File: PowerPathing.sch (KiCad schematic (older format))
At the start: 23 parts, among them IC1 LTC4372IMS8#TRPBF, IC2 L4940D2T12-TR, IC3 MAX738ACWE+, Q1 BSC026NE2LS5ATMA1

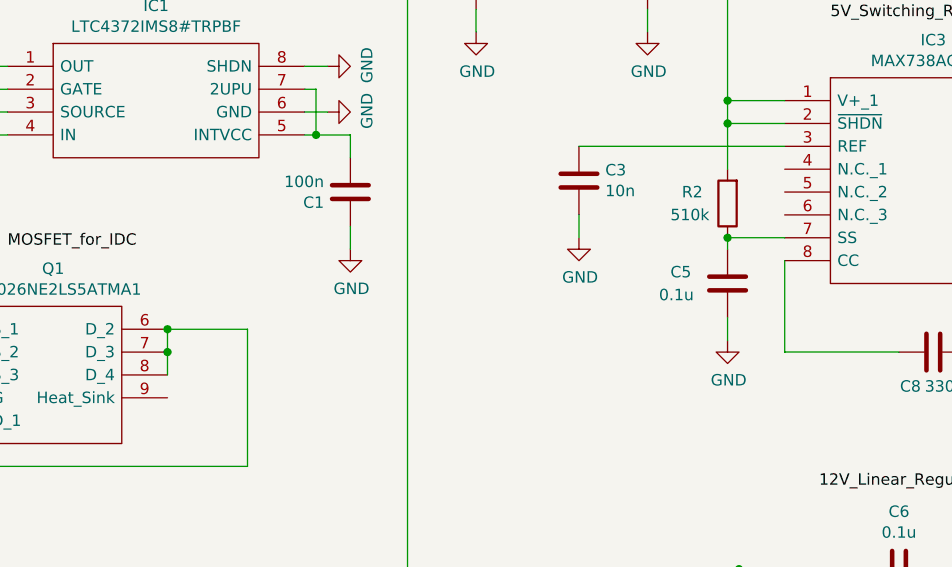
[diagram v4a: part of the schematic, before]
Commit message: added connector to schematic
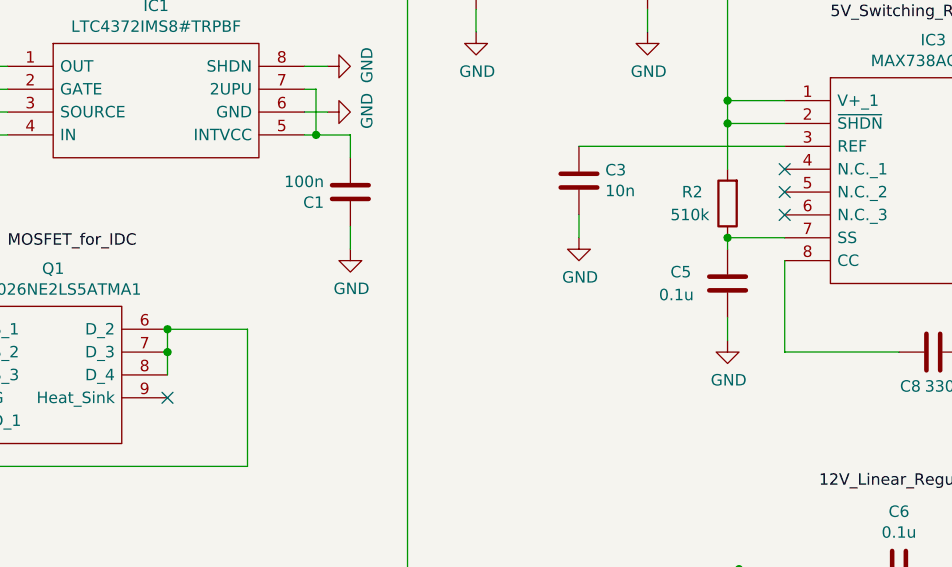
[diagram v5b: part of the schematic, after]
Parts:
- C1, C3, C5, C6, C8: footprint (none) -> Capacitor_SMD:C_0805_2012Metric_Pad1.18x1.45mm_HandSolder
- D1: footprint (none) -> Diode_SMD:D_0805_2012Metric_Pad1.15x1.40mm_HandSolder
- R1, R2: footprint (none) -> Resistor_SMD:R_0805_2012Metric_Pad1.20x1.40mm_HandSolder
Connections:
- no-connect marks 0 -> 4
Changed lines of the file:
@@
 F 0 "C3" H 4865 2846 50  0000 L CNN
 F 1 "10n" H 4865 2755 50  0000 L CNN
-F 2 "" H 4788 2650 50  0001 C CNN
+F 2 "Capacitor_SMD:C_0805_2012Metric_Pad1.18x1.45mm_HandSolder" H 4788 2650 50  0001 C CNN
 F 3 "~" H 4750 2800 50  0001 C CNN
 	1    4750 2800
@@
 F 0 "R2" H 5600 2850 50  0000 R CNN
 F 1 "510k" H 5650 2950 50  0000 R CNN
-F 2 "" V 5330 2900 50  0001 C CNN
+F 2 "Resistor_SMD:R_0805_2012Metric_Pad1.20x1.40mm_HandSolder" V 5330 2900 50  0001 C CNN
 F 3 "~" H 5400 2900 50  0001 C CNN
 	1    5400 2900
@@
 F 0 "C5" H 5150 3300 50  0000 L CNN
 F 1 "0.1u" H 5100 3200 50  0000 L CNN
-F 2 "" H 5438 3100 50  0001 C CNN
+F 2 "Capacitor_SMD:C_0805_2012Metric_Pad1.18x1.45mm_HandSolder" H 5438 3100 50  0001 C CNN
 F 3 "~" H 5400 3250 50  0001 C CNN
 	1    5400 3250
@@
 F 0 "C8" V 6450 3450 50  0000 C CNN
 F 1 "330p" V 6450 3600 50  0000 C CNN
-F 2 "" H 6338 3400 50  0001 C CNN
+F 2 "Capacitor_SMD:C_0805_2012Metric_Pad1.18x1.45mm_HandSolder" H 6338 3400 50  0001 C CNN
 F 3 "~" H 6300 3550 50  0001 C CNN
 	1    6300 3550
@@
 F 0 "C6" V 5898 4500 50  0000 C CNN
 F 1 "0.1u" V 5989 4500 50  0000 C CNN
-F 2 "" H 6188 4350 50  0001 C CNN
+F 2 "Capacitor_SMD:C_0805_2012Metric_Pad1.18x1.45mm_HandSolder" H 6188 4350 50  0001 C CNN
 F 3 "~" H 6150 4500 50  0001 C CNN
 	1    6150 4500
@@
 F 0 "C1" H 3865 2896 50  0000 L CNN
 F 1 "100n" H 3865 2805 50  0000 L CNN
-F 2 "" H 3788 2700 50  0001 C CNN
+F 2 "Capacitor_SMD:C_0805_2012Metric_Pad1.18x1.45mm_HandSolder" H 3788 2700 50  0001 C CNN
 F 3 "~" H 3750 2850 50  0001 C CNN
 	1    3750 2850
@@
 F 0 "R1" H 1670 2096 50  0000 L CNN
 F 1 "111 ohms" H 1670 2005 50  0000 L CNN
-F 2 "" V 1530 2050 50  0001 C CNN
+F 2 "Resistor_SMD:R_0805_2012Metric_Pad1.20x1.40mm_HandSolder" V 1530 2050 50  0001 C CNN
 F 3 "~" H 1600 2050 50  0001 C CNN
 	1    1600 2050
@@
 F 0 "D1" H 1300 1533 50  0000 C CNN
 F 1 "1N4001G" H 1300 1624 50  0000 C CNN
-F 2 "" H 1300 1750 50  0001 C CNN
+F 2 "Diode_SMD:D_0805_2012Metric_Pad1.15x1.40mm_HandSolder" H 1300 1750 50  0001 C CNN
 F 3 "~" H 1300 1750 50  0001 C CNN
 	1    1300 1750
@@
 Text Label 2250 3100 0    50   ~ 0
 MOSFET_for_IDC
+NoConn ~ 2950 3750
+NoConn ~ 5650 2950
+NoConn ~ 5650 2850
+NoConn ~ 5650 2750
 $EndSCHEMATC

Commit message: Started schematic development
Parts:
- removed C4: 1u, symbol Device:CP
- added C4: 860020672005, CAPPRD200W52D500H1250, symbol Capstone:860020672005
- C1, C3, C5, C6, C8: footprint Capacitor_SMD:C_0805_2012Metric_Pad1.18x1.45mm_HandSolder -> Capacitor_THT:C_Rect_L7.0mm_W2.5mm_P5.00mm
- C2: footprint (none) -> CAPPRD200W52D500H1250
- C7, C9: footprint (none) -> Capstone:CAPPRD200W52D500H1250
- R1: value 111 ohms -> 111; footprint Resistor_SMD:R_0805_2012Metric_Pad1.20x1.40mm_HandSolder -> Resistor_THT:R_Axial_DIN0204_L3.6mm_D1.6mm_P7.62mm_Horizontal
- R2: footprint Resistor_SMD:R_0805_2012Metric_Pad1.20x1.40mm_HandSolder -> Resistor_THT:R_Axial_DIN0204_L3.6mm_D1.6mm_P7.62mm_Horizontal
- TP1, TP2, TP3, TP4, TP5: footprint (none) -> TestPoint:TestPoint_Loop_D2.60mm_Drill1.6mm_Beaded
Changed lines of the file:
@@
 F 0 "C9" H 9518 2946 50  0000 L CNN
 F 1 "100u" H 9518 2855 50  0000 L CNN
-F 2 "" H 9438 2750 50  0001 C CNN
+F 2 "Capstone:CAPPRD200W52D500H1250" H 9438 2750 50  0001 C CNN
 F 3 "~" H 9400 2900 50  0001 C CNN
 	1    9400 2900
 	1    0    0    -1
 $EndComp
-$Comp
-L Device:CP C4
-U 1 1 61549C3D
-P 5050 1900
-F 0 "C4" H 5168 1946 50  0000 L CNN
-F 1 "1u" H 5168 1855 50  0000 L CNN
-F 2 "" H 5088 1750 50  0001 C CNN
-F 3 "~" H 5050 1900 50  0001 C CNN
-	1    5050 1900
-	1    0    0    -1
-$EndComp
-Wire Wire Line
-	5050 1750 5400 1750
 Wire Wire Line
 	5400 1750 5400 2450
 Wire Wire Line
 	5400 2450 5650 2450
-Connection ~ 5050 1750
 Wire Wire Line
 	5650 2550 5400 2550
@@
 F 0 "C3" H 4865 2846 50  0000 L CNN
 F 1 "10n" H 4865 2755 50  0000 L CNN
-F 2 "Capacitor_SMD:C_0805_2012Metric_Pad1.18x1.45mm_HandSolder" H 4788 2650 50  0001 C CNN
+F 2 "Capacitor_THT:C_Rect_L7.0mm_W2.5mm_P5.00mm" H 4788 2650 50  0001 C CNN
 F 3 "~" H 4750 2800 50  0001 C CNN
 	1    4750 2800
@@
 F 0 "R2" H 5600 2850 50  0000 R CNN
 F 1 "510k" H 5650 2950 50  0000 R CNN
-F 2 "Resistor_SMD:R_0805_2012Metric_Pad1.20x1.40mm_HandSolder" V 5330 2900 50  0001 C CNN
+F 2 "Resistor_THT:R_Axial_DIN0204_L3.6mm_D1.6mm_P7.62mm_Horizontal" V 5330 2900 50  0001 C CNN
 F 3 "~" H 5400 2900 50  0001 C CNN
 	1    5400 2900
@@
 F 0 "C5" H 5150 3300 50  0000 L CNN
 F 1 "0.1u" H 5100 3200 50  0000 L CNN
-F 2 "Capacitor_SMD:C_0805_2012Metric_Pad1.18x1.45mm_HandSolder" H 5438 3100 50  0001 C CNN
+F 2 "Capacitor_THT:C_Rect_L7.0mm_W2.5mm_P5.00mm" H 5438 3100 50  0001 C CNN
 F 3 "~" H 5400 3250 50  0001 C CNN
 	1    5400 3250
@@
 F 0 "C8" V 6450 3450 50  0000 C CNN
 F 1 "330p" V 6450 3600 50  0000 C CNN
-F 2 "Capacitor_SMD:C_0805_2012Metric_Pad1.18x1.45mm_HandSolder" H 6338 3400 50  0001 C CNN
+F 2 "Capacitor_THT:C_Rect_L7.0mm_W2.5mm_P5.00mm" H 6338 3400 50  0001 C CNN
 F 3 "~" H 6300 3550 50  0001 C CNN
 	1    6300 3550
@@
 F 0 "C6" V 5898 4500 50  0000 C CNN
 F 1 "0.1u" V 5989 4500 50  0000 C CNN
-F 2 "Capacitor_SMD:C_0805_2012Metric_Pad1.18x1.45mm_HandSolder" H 6188 4350 50  0001 C CNN
+F 2 "Capacitor_THT:C_Rect_L7.0mm_W2.5mm_P5.00mm" H 6188 4350 50  0001 C CNN
 F 3 "~" H 6150 4500 50  0001 C CNN
 	1    6150 4500
@@
 F 0 "C7" V 5900 5350 50  0000 C CNN
 F 1 "22u" V 6000 5350 50  0000 C CNN
-F 2 "" H 6188 5200 50  0001 C CNN
+F 2 "Capstone:CAPPRD200W52D500H1250" H 6188 5200 50  0001 C CNN
 F 3 "~" H 6150 5350 50  0001 C CNN
 	1    6150 5350
@@
 F 0 "C2" H 4418 1946 50  0000 L CNN
 F 1 "68u" H 4418 1855 50  0000 L CNN
-F 2 "" H 4338 1750 50  0001 C CNN
+F 2 "CAPPRD200W52D500H1250" H 4338 1750 50  0001 C CNN
 F 3 "~" H 4300 1900 50  0001 C CNN
 	1    4300 1900
@@
 $EndComp
 Connection ~ 4300 1750
-Wire Wire Line
-	4300 1750 5050 1750
 $Comp
 L Capstone:LTC4372IMS8#TRPBF IC1
@@
 F 0 "C1" H 3865 2896 50  0000 L CNN
 F 1 "100n" H 3865 2805 50  0000 L CNN
-F 2 "Capacitor_SMD:C_0805_2012Metric_Pad1.18x1.45mm_HandSolder" H 3788 2700 50  0001 C CNN
+F 2 "Capacitor_THT:C_Rect_L7.0mm_W2.5mm_P5.00mm" H 3788 2700 50  0001 C CNN
 F 3 "~" H 3750 2850 50  0001 C CNN
 	1    3750 2850
@@
 P 1600 2050
 F 0 "R1" H 1670 2096 50  0000 L CNN
-F 1 "111 ohms" H 1670 2005 50  0000 L CNN
-F 2 "Resistor_SMD:R_0805_2012Metric_Pad1.20x1.40mm_HandSolder" V 1530 2050 50  0001 C CNN
+F 1 "111" H 1670 2005 50  0000 L CNN
+F 2 "Resistor_THT:R_Axial_DIN0204_L3.6mm_D1.6mm_P7.62mm_Horizontal" V 1530 2050 50  0001 C CNN
 F 3 "~" H 1600 2050 50  0001 C CNN
 	1    1600 2050
@@
 F 0 "TP2" H 4192 5276 50  0000 R CNN
 F 1 "TestPoint - 12V Reg" H 4192 5367 50  0000 R CNN
-F 2 "" H 4450 5250 50  0001 C CNN
+F 2 "TestPoint:TestPoint_Loop_D2.60mm_Drill1.6mm_Beaded" H 4450 5250 50  0001 C CNN
 F 3 "~" H 4450 5250 50  0001 C CNN
 	1    4250 5250
@@
 F 0 "TP5" H 10208 2718 50  0000 L CNN
 F 1 "TestPoint - 5V Reg" H 10208 2627 50  0000 L CNN
-F 2 "" H 10350 2600 50  0001 C CNN
+F 2 "TestPoint:TestPoint_Loop_D2.60mm_Drill1.6mm_Beaded" H 10350 2600 50  0001 C CNN
 F 3 "~" H 10350 2600 50  0001 C CNN
 	1    10150 2600
@@
 F 0 "TP1" H 3658 1668 50  0000 L CNN
 F 1 "TestPoint - Power Circuit Out" H 3658 1577 50  0000 L CNN
-F 2 "" H 3800 1550 50  0001 C CNN
+F 2 "TestPoint:TestPoint_Loop_D2.60mm_Drill1.6mm_Beaded" H 3800 1550 50  0001 C CNN
 F 3 "~" H 3800 1550 50  0001 C CNN
 	1    3600 1550
@@
 L power:GND #PWR0105
 U 1 1 616ACF0A
-P 5050 2150
-F 0 "#PWR0105" H 5050 1900 50  0001 C CNN
-F 1 "GND" H 5055 1977 50  0000 C CNN
-F 2 "" H 5050 2150 50  0001 C CNN
-F 3 "" H 5050 2150 50  0001 C CNN
-	1    5050 2150
-	1    0    0    -1
-$EndComp
-Wire Wire Line
-	5050 2150 5050 2050
+P 5050 2300
+F 0 "#PWR0105" H 5050 2050 50  0001 C CNN
+F 1 "GND" H 5055 2127 50  0000 C CNN
+F 2 "" H 5050 2300 50  0001 C CNN
+F 3 "" H 5050 2300 50  0001 C CNN
+	1    5050 2300
+	1    0    0    -1
+$EndComp
 $Comp
 L power:GND #PWR0106
@@
 F 0 "TP4" H 7000 3400 50  0000 L CNN
 F 1 "GND 5V Reg" H 6800 3500 50  0000 L CNN
-F 2 "" H 7400 3250 50  0001 C CNN
+F 2 "TestPoint:TestPoint_Loop_D2.60mm_Drill1.6mm_Beaded" H 7400 3250 50  0001 C CNN
 F 3 "~" H 7400 3250 50  0001 C CNN
 	1    7200 3250
@@
 F 0 "TP3" V 7104 5338 50  0000 L CNN
 F 1 "GND 12V Reg" V 7195 5338 50  0000 L CNN
-F 2 "" H 7350 5150 50  0001 C CNN
+F 2 "TestPoint:TestPoint_Loop_D2.60mm_Drill1.6mm_Beaded" H 7350 5150 50  0001 C CNN
 F 3 "~" H 7350 5150 50  0001 C CNN
 	1    7150 5150
@@
 NoConn ~ 5650 2850
 NoConn ~ 5650 2750
+Wire Wire Line
+	4300 1750 5050 1750
+$Comp
+L Capstone:860020672005 C4
+U 1 1 61629E3D
+P 5050 1750
+F 0 "C4" V 5250 1500 50  0000 L CNN
+F 1 "860020672005" V 5400 1100 50  0000 L CNN
+F 2 "CAPPRD200W52D500H1250" H 5400 1800 50  0001 L CNN
+F 3 "https://componentsearchengine.com/Datasheets/2/860020672005.pdf" H 5400 1700 50  0001 L CNN
+F 4 "Wurth Elektronik 1uF 50 V dc Aluminium Electrolytic Capacitor, WCAP-ATG5 Series 2000h 5 (Dia.) x 11mm" H 5400 1600 50  0001 L CNN "Description"
+F 5 "12.5" H 5400 1500 50  0001 L CNN "Height"
+F 6 "Wurth Elektronik" H 5400 1400 50  0001 L CNN "Manufacturer_Name"
+F 7 "860020672005" H 5400 1300 50  0001 L CNN "Manufacturer_Part_Number"
+F 8 "710-860020672005" H 5400 1200 50  0001 L CNN "Mouser Part Number"
+F 9 "https://www.mouser.co.uk/ProductDetail/Wurth-Elektronik/860020672005?qs=0KOYDY2FL29w5cS8aahRvQ%3D%3D" H 5400 1100 50  0001 L CNN "Mouser Price/Stock"
+F 10 "" H 5400 1000 50  0001 L CNN "Arrow Part Number"
+F 11 "" H 5400 900 50  0001 L CNN "Arrow Price/Stock"
+	1    5050 1750
+	0    1    1    0
+$EndComp
+Connection ~ 5050 1750
+Wire Wire Line
+	5050 1750 5400 1750
+Wire Wire Line
+	5050 2300 5050 2250
 $EndSCHEMATC

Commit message: initial commit for layout
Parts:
- R1, R2: footprint Resistor_THT:R_Axial_DIN0204_L3.6mm_D1.6mm_P7.62mm_Horizontal -> Capstone:RESAD1650W60L650D250
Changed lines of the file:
@@
 F 0 "R2" H 5600 2850 50  0000 R CNN
 F 1 "510k" H 5650 2950 50  0000 R CNN
-F 2 "Resistor_THT:R_Axial_DIN0204_L3.6mm_D1.6mm_P7.62mm_Horizontal" V 5330 2900 50  0001 C CNN
+F 2 "Capstone:RESAD1650W60L650D250" V 5330 2900 50  0001 C CNN
 F 3 "~" H 5400 2900 50  0001 C CNN
 	1    5400 2900
@@
 F 0 "R1" H 1670 2096 50  0000 L CNN
 F 1 "111" H 1670 2005 50  0000 L CNN
-F 2 "Resistor_THT:R_Axial_DIN0204_L3.6mm_D1.6mm_P7.62mm_Horizontal" V 1530 2050 50  0001 C CNN
+F 2 "Capstone:RESAD1650W60L650D250" V 1530 2050 50  0001 C CNN
 F 3 "~" H 1600 2050 50  0001 C CNN
 	1    1600 2050

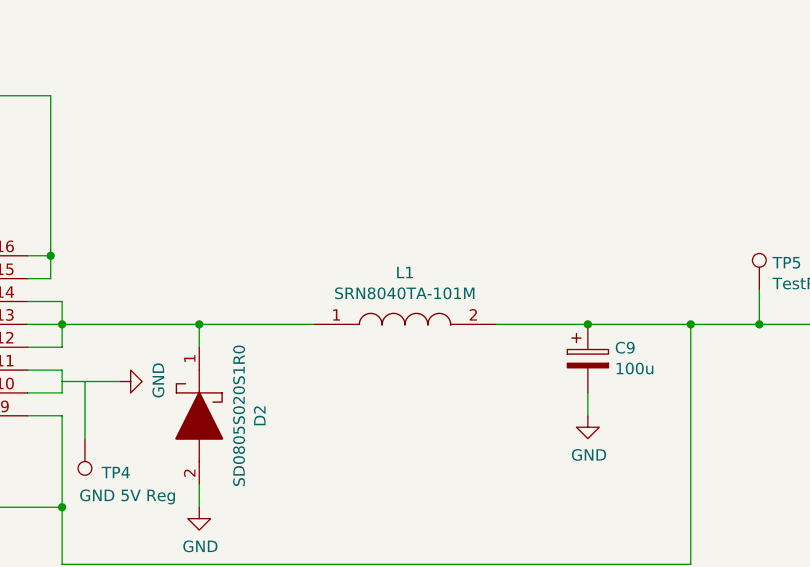
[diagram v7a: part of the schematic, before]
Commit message: changed inductor used in power circuitry
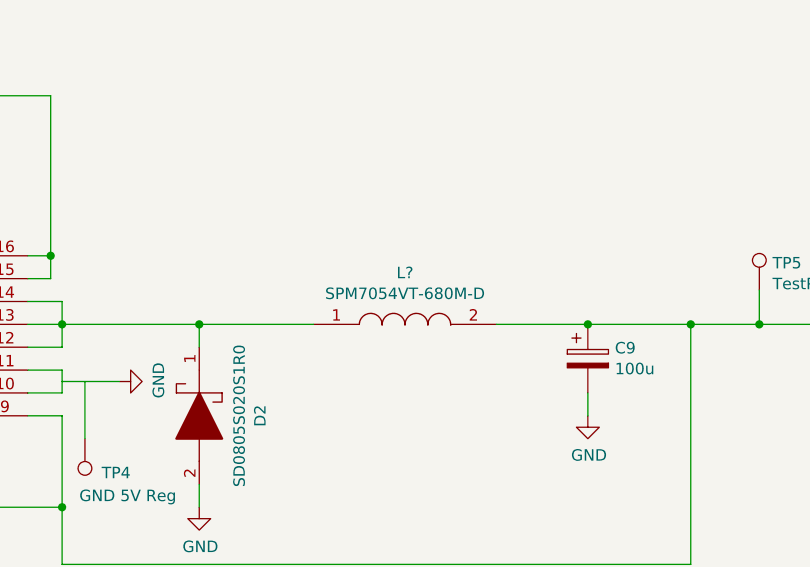
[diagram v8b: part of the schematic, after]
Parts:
- removed L1: SRN8040TA-101M, INDPM8080X450N, symbol Capstone:SRN8040TA-101M
- added L?: SPM7054VT-680M-D, SPM7054VT, symbol Capstone:SPM7054VT-680M-D
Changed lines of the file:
@@
 Wire Wire Line
 	7700 2750 8200 2750
-$Comp
-L Capstone:SRN8040TA-101M L1
-U 1 1 61561B3F
-P 8200 2750
-F 0 "L1" H 8600 2975 50  0000 C CNN
-F 1 "SRN8040TA-101M" H 8600 2884 50  0000 C CNN
-F 2 "INDPM8080X450N" H 8850 2800 50  0001 L CNN
-F 3 "http://www.bourns.com/docs/Product-Datasheets/SRN8040TA.pdf" H 8850 2700 50  0001 L CNN
-F 4 "fixed Inductor 100uH 1.1A non-Shielded" H 8850 2600 50  0001 L CNN "Description"
-F 5 "4.5" H 8850 2500 50  0001 L CNN "Height"
-F 6 "Bourns" H 8850 2400 50  0001 L CNN "Manufacturer_Name"
-F 7 "SRN8040TA-101M" H 8850 2300 50  0001 L CNN "Manufacturer_Part_Number"
-F 8 "652-SRN8040TA-101M" H 8850 2200 50  0001 L CNN "Mouser Part Number"
-F 9 "https://www.mouser.co.uk/ProductDetail/Bourns/SRN8040TA-101M?qs=Vt59ZOdFuWYPicTq%2FhiccQ%3D%3D" H 8850 2100 50  0001 L CNN "Mouser Price/Stock"
-F 10 "SRN8040TA-101M" H 8850 2000 50  0001 L CNN "Arrow Part Number"
-F 11 "https://www.arrow.com/en/products/srn8040ta-101m/bourns" H 8850 1900 50  0001 L CNN "Arrow Price/Stock"
-	1    8200 2750
-	1    0    0    -1
-$EndComp
 Wire Wire Line
 	9000 2750 9400 2750
@@
 Wire Wire Line
 	5050 2300 5050 2250
+$Comp
+L Capstone:SPM7054VT-680M-D L?
+U 1 1 6167E1EA
+P 8200 2750
+F 0 "L?" H 8600 2975 50  0000 C CNN
+F 1 "SPM7054VT-680M-D" H 8600 2884 50  0000 C CNN
+F 2 "SPM7054VT" H 8850 2800 50  0001 L CNN
+F 3 "https://product.tdk.com/system/files/dam/doc/product/inductor/inductor/smd/catalog/inductor_automotive_power_spm7054vt-d_en.pdf" H 8850 2700 50  0001 L CNN
+F 4 "Inductors for power circuits, Wound metal, Automotive" H 8850 2600 50  0001 L CNN "Description"
+F 5 "" H 8850 2500 50  0001 L CNN "Height"
+F 6 "TDK" H 8850 2400 50  0001 L CNN "Manufacturer_Name"
+F 7 "SPM7054VT-680M-D" H 8850 2300 50  0001 L CNN "Manufacturer_Part_Number"
+F 8 "810-SPM7054VT-680M-D" H 8850 2200 50  0001 L CNN "Mouser Part Number"
+F 9 "https://www.mouser.co.uk/ProductDetail/TDK/SPM7054VT-680M-D?qs=BJlw7L4Cy7%2F5GJUhXb8MnA%3D%3D" H 8850 2100 50  0001 L CNN "Mouser Price/Stock"
+F 10 "" H 8850 2000 50  0001 L CNN "Arrow Part Number"
+F 11 "" H 8850 1900 50  0001 L CNN "Arrow Price/Stock"
+	1    8200 2750
+	1    0    0    -1
+$EndComp
 $EndSCHEMATC
